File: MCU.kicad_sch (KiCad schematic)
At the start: 8 parts, among them U2 BL652

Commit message: Misc updates and tweak. Work still needed, letf notes in top schematic page
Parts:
- added J1: Conn_ARM_SWD_TagConnect_TC2030-NL, Connector:Tag-Connect_TC2030-IDC-NL_2x03_P1.27mm_Vertical, symbol Connector:Conn_ARM_SWD_TagConnect_TC2030-NL
- R1, R2: value R -> 100K
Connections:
- net +3V3: now also J1.1 (VCC)
- net Audio_FIL: no longer U2.29 (SIO_15)
- net Audio_RAW: no longer U2.28 (SIO_13)
- net GND: now also J1.5 (GND)
- net Intensity_Dial: no longer U2.4 (SIO_22)
- net SWDIO: now reaches U2.5 (SWDIO)
- net SWDIO: now also J1.2 (SWDIO)
- net SWCLK: now reaches U2.6 (SWDCLK)
- net SWCLK: now also J1.4 (SWCLK)
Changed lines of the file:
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@@
+    (stroke (width 0) (type default))
+  )
+  (wire (pts (xy 154.94 33.02) (xy 162.56 33.02))
     (stroke (width 0) (type default))
   )
@@
     (stroke (width 0) (type default))
   )
+  (wire (pts (xy 144.78 43.18) (xy 144.78 44.45))
+    (stroke (width 0) (type default))
+  )
   (wire (pts (xy 87.63 105.41) (xy 104.14 105.41))
     (stroke (width 0) (type default))
@@
   )
   (wire (pts (xy 154.94 90.17) (xy 190.5 90.17))
+    (stroke (width 0) (type default))
+  )
+  (wire (pts (xy 154.94 35.56) (xy 162.56 35.56))
     (stroke (width 0) (type default))
   )
@@
     (effects (font (size 1.27 1.27)) (justify left bottom))
   )
+  (label "SWDIO" (at 154.94 82.55 0) (fields_autoplaced)
+    (effects (font (size 1.27 1.27)) (justify left bottom))
+  )
+  (label "SWCLK" (at 154.94 80.01 0) (fields_autoplaced)
+    (effects (font (size 1.27 1.27)) (justify left bottom))
+  )
+  (label "SWCLK" (at 156.21 33.02 0) (fields_autoplaced)
+    (effects (font (size 1.27 1.27)) (justify left bottom))
+  )
   (label "RES2" (at 87.63 105.41 0) (fields_autoplaced)
     (effects (font (size 1.27 1.27)) (justify left bottom))
   )
   (label "RES" (at 87.63 102.87 0) (fields_autoplaced)
+    (effects (font (size 1.27 1.27)) (justify left bottom))
+  )
+  (label "SWDIO" (at 156.21 35.56 0) (fields_autoplaced)
     (effects (font (size 1.27 1.27)) (justify left bottom))
   )
@@
     (effects (font (size 1.27 1.27)) (justify left))
   )
-  (hierarchical_label "Audio_RAW" (shape input) (at 104.14 113.03 180) (fields_autoplaced)
+  (hierarchical_label "Audio_RAW" (shape input) (at 83.82 74.93 180) (fields_autoplaced)
     (effects (font (size 1.27 1.27)) (justify right))
   )
@@
     (effects (font (size 1.27 1.27)) (justify left))
   )
-  (hierarchical_label "Audio_FIL" (shape input) (at 104.14 118.11 180) (fields_autoplaced)
+  (hierarchical_label "Audio_FIL" (shape input) (at 82.55 78.74 180) (fields_autoplaced)
     (effects (font (size 1.27 1.27)) (justify right))
   )
@@
     (effects (font (size 1.27 1.27)) (justify right))
   )
-  (hierarchical_label "Intensity_Dial" (shape input) (at 154.94 113.03 0) (fields_autoplaced)
+  (hierarchical_label "Intensity_Dial" (shape input) (at 72.39 71.12 0) (fields_autoplaced)
     (effects (font (size 1.27 1.27)) (justify left))
   )
@@
       (effects (font (size 1.27 1.27)) (justify left))
     )
-    (property "Value" "R" (at 193.04 87.63 0)
+    (property "Value" "100K" (at 193.04 87.63 0)
       (effects (font (size 1.27 1.27)) (justify left))
     )
@@
         (path "/704dec10-a4c2-4298-be85-193d9407f59f/a98cecf9-ef60-4d48-8d8f-6fc42778f104"
           (reference "R1") (unit 1)
+        )
+      )
+    )
+  )
+  (symbol (lib_id "power:+3V3") (at 144.78 22.86 0) (unit 1)
+    (in_bom yes) (on_board yes) (dnp no) (fields_autoplaced)
+    (property "Reference" "#PWR039" (at 144.78 26.67 0)
+      (effects (font (size 1.27 1.27)) hide)
+    )
+    (property "Value" "+3V3" (at 144.78 17.78 0)
+      (effects (font (size 1.27 1.27)))
+    )
+    (property "Footprint" "" (at 144.78 22.86 0)
+      (effects (font (size 1.27 1.27)) hide)
+    )
+    (property "Datasheet" "" (at 144.78 22.86 0)
+      (effects (font (size 1.27 1.27)) hide)
+    )
+    (pin "1")
+    (instances
+      (project "VibeLight"
+        (path "/704dec10-a4c2-4298-be85-193d9407f59f/a98cecf9-ef60-4d48-8d8f-6fc42778f104"
+          (reference "#PWR039") (unit 1)
+        )
+      )
+    )
+  )
+  (symbol (lib_id "power:GND") (at 144.78 44.45 0) (unit 1)
+    (in_bom yes) (on_board yes) (dnp no) (fields_autoplaced)
+    (property "Reference" "#PWR040" (at 144.78 50.8 0)
+      (effects (font (size 1.27 1.27)) hide)
+    )
+    (property "Value" "GND" (at 144.78 49.53 0)
+      (effects (font (size 1.27 1.27)))
+    )
+    (property "Footprint" "" (at 144.78 44.45 0)
+      (effects (font (size 1.27 1.27)) hide)
+    )
+    (property "Datasheet" "" (at 144.78 44.45 0)
+      (effects (font (size 1.27 1.27)) hide)
+    )
+    (pin "1")
+    (instances
+      (project "VibeLight"
+        (path "/704dec10-a4c2-4298-be85-193d9407f59f/a98cecf9-ef60-4d48-8d8f-6fc42778f104"
+          (reference "#PWR040") (unit 1)
         )
       )
@@
     )
   )
+  (symbol (lib_id "Connector:Conn_ARM_SWD_TagConnect_TC2030-NL") (at 147.32 33.02 0) (unit 1)
+    (in_bom no) (on_board yes) (dnp no) (fields_autoplaced)
+    (property "Reference" "J1" (at 140.97 31.75 0)
+      (effects (font (size 1.27 1.27)) (justify right))
+    )
+    (property "Value" "Conn_ARM_SWD_TagConnect_TC2030-NL" (at 140.97 34.29 0)
+      (effects (font (size 1.27 1.27)) (justify right))
+    )
+    (property "Footprint" "Connector:Tag-Connect_TC2030-IDC-NL_2x03_P1.27mm_Vertical" (at 147.32 50.8 0)
+      (effects (font (size 1.27 1.27)) hide)
+    )
+    (property "Datasheet" "https://www.tag-connect.com/wp-content/uploads/bsk-pdf-manager/TC2030-CTX_1.pdf" (at 147.32 48.26 0)
+      (effects (font (size 1.27 1.27)) hide)
+    )
+    (pin "1")
+    (pin "2")
+    (pin "3")
+    (pin "4")
+    (pin "5")
+    (pin "6")
+    (instances
+      (project "VibeLight"
+        (path "/704dec10-a4c2-4298-be85-193d9407f59f/a98cecf9-ef60-4d48-8d8f-6fc42778f104"
+          (reference "J1") (unit 1)
+        )
+      )
+    )
+  )
   (symbol (lib_id "power:GND") (at 190.5 97.79 0) (unit 1)
     (in_bom yes) (on_board yes) (dnp no) (fields_autoplaced)
@@
       (effects (font (size 1.27 1.27)) (justify left))
     )
-    (property "Value" "R" (at 193.04 95.25 0)
-      (effects (font (size 1.27 1.27)) (justify left))
-    )
+    (property "Value" "100K" (at 193.04 95.25 0)
+      (effects (font (size 1.27 1.27)) (justify left))
+    )

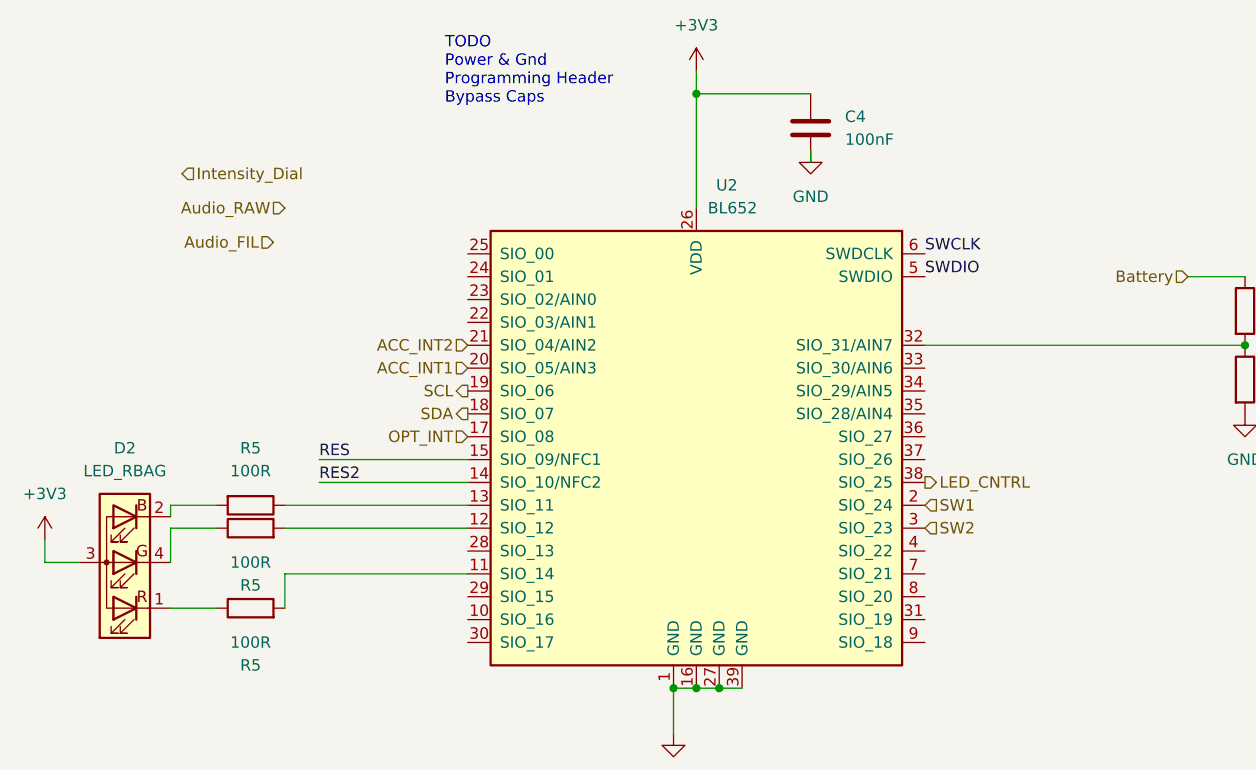
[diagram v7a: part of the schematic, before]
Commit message: update
updated in accordance with 8/5 schem notes
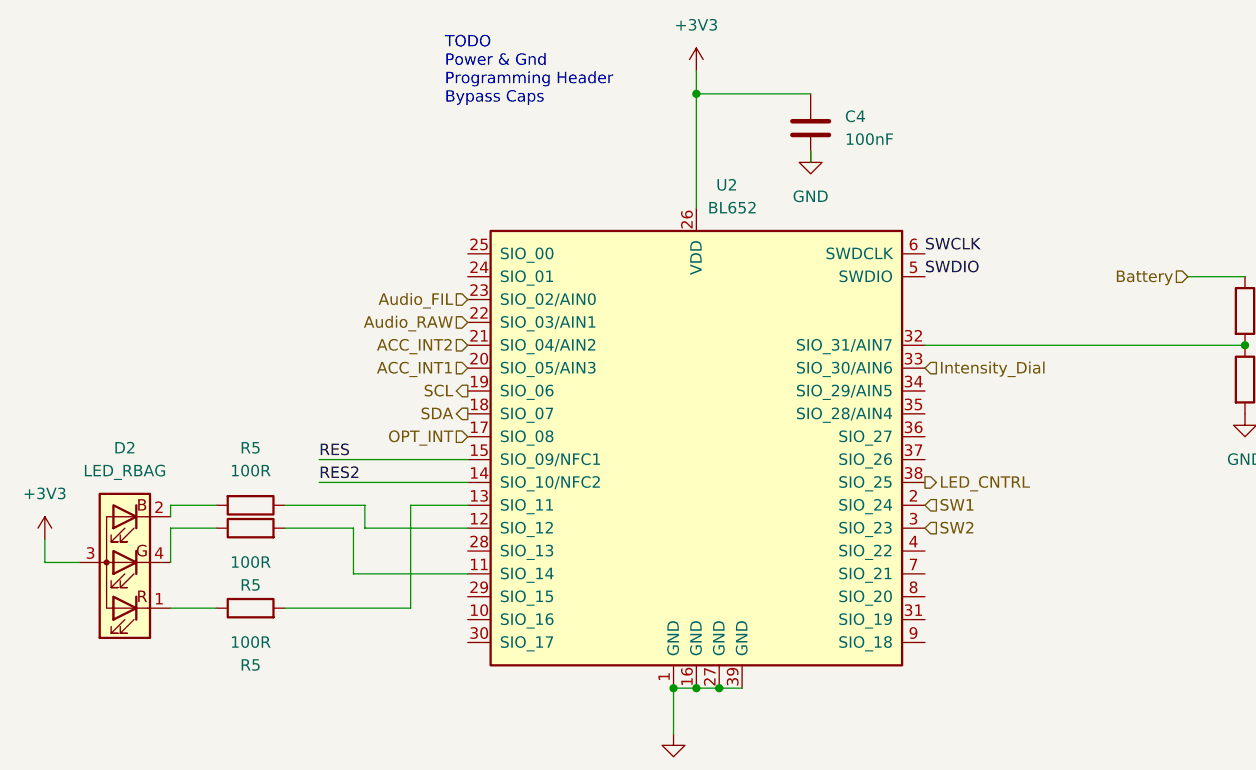
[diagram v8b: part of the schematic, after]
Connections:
- net Audio_FIL: now also U2.23 (SIO_02/AIN0)
- net Audio_RAW: now also U2.22 (SIO_03/AIN1)
- net Intensity_Dial: now also U2.33 (SIO_30/AIN6)
- net at R5.2: now also U2.13 (SIO_11); no longer U2.11 (SIO_14)
- net at R5.2: now also U2.11 (SIO_14); no longer U2.12 (SIO_12)
- net at R5.1: now also U2.12 (SIO_12); no longer U2.13 (SIO_11)
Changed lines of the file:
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@@
+    (stroke (width 0) (type default))
+  )
+  (wire (pts (xy 92.71 107.95) (xy 92.71 110.49))
     (stroke (width 0) (type default))
   )
   (wire (pts (xy 71.12 119.38) (xy 76.2 119.38))
+    (stroke (width 0) (type default))
+  )
+  (wire (pts (xy 83.82 110.49) (xy 91.44 110.49))
     (stroke (width 0) (type default))
   )
@@
     (stroke (width 0) (type default))
   )
-  (wire (pts (xy 83.82 119.38) (xy 83.82 115.57))
-    (stroke (width 0) (type default))
-  )
   (wire (pts (xy 60.96 114.3) (xy 57.15 114.3))
     (stroke (width 0) (type default))
   )
-  (wire (pts (xy 83.82 107.95) (xy 104.14 107.95))
+  (wire (pts (xy 97.79 107.95) (xy 104.14 107.95))
     (stroke (width 0) (type default))
   )
@@
     (stroke (width 0) (type default))
   )
+  (wire (pts (xy 83.82 119.38) (xy 97.79 119.38))
+    (stroke (width 0) (type default))
+  )
   (wire (pts (xy 71.12 107.95) (xy 76.2 107.95))
     (stroke (width 0) (type default))
   )
   (wire (pts (xy 71.12 109.22) (xy 71.12 107.95))
+    (stroke (width 0) (type default))
+  )
+  (wire (pts (xy 97.79 119.38) (xy 97.79 107.95))
     (stroke (width 0) (type default))
   )
@@
     (stroke (width 0) (type default))
   )
+  (wire (pts (xy 83.82 107.95) (xy 92.71 107.95))
+    (stroke (width 0) (type default))
+  )
+  (wire (pts (xy 91.44 110.49) (xy 91.44 115.57))
+    (stroke (width 0) (type default))
+  )
+  (wire (pts (xy 91.44 115.57) (xy 104.14 115.57))
+    (stroke (width 0) (type default))
+  )
   (wire (pts (xy 87.63 105.41) (xy 104.14 105.41))
     (stroke (width 0) (type default))
   )
-  (wire (pts (xy 83.82 110.49) (xy 104.14 110.49))
-    (stroke (width 0) (type default))
-  )
   (wire (pts (xy 71.12 114.3) (xy 71.12 110.49))
-    (stroke (width 0) (type default))
-  )
-  (wire (pts (xy 83.82 115.57) (xy 104.14 115.57))
     (stroke (width 0) (type default))
   )
@@
   )
   (wire (pts (xy 154.94 90.17) (xy 190.5 90.17))
+    (stroke (width 0) (type default))
+  )
+  (wire (pts (xy 92.71 110.49) (xy 104.14 110.49))
     (stroke (width 0) (type default))
   )
@@
     (effects (font (size 1.27 1.27)) (justify left))
   )
-  (hierarchical_label "Audio_RAW" (shape input) (at 83.82 74.93 180) (fields_autoplaced)
+  (hierarchical_label "Audio_RAW" (shape input) (at 104.14 87.63 180) (fields_autoplaced)
     (effects (font (size 1.27 1.27)) (justify right))
   )
@@
     (effects (font (size 1.27 1.27)) (justify left))
   )
-  (hierarchical_label "Audio_FIL" (shape input) (at 82.55 78.74 180) (fields_autoplaced)
+  (hierarchical_label "Audio_FIL" (shape input) (at 104.14 85.09 180) (fields_autoplaced)
     (effects (font (size 1.27 1.27)) (justify right))
   )
@@
     (effects (font (size 1.27 1.27)) (justify right))
   )
-  (hierarchical_label "Intensity_Dial" (shape input) (at 72.39 71.12 0) (fields_autoplaced)
+  (hierarchical_label "Intensity_Dial" (shape input) (at 154.94 92.71 0) (fields_autoplaced)
     (effects (font (size 1.27 1.27)) (justify left))
   )
